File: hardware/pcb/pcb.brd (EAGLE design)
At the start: 100 x 80 mm, 18 parts, among them IC1 LM1117MPX-ADJ

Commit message: added support for new new display
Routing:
- net GND: track 0.00 -> 10.2 mm
- net N$11: track 0.00 -> 1.84 mm
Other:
- board size 100 x 80 mm -> 51.7 x 80 mm
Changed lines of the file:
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@@
 <board>
 <plain>
-<wire x1="0" y1="0" x2="100" y2="0" width="0" layer="20"/>
+<wire x1="48.26" y1="0" x2="100" y2="0" width="0" layer="20"/>
 <wire x1="100" y1="0" x2="100" y2="80" width="0" layer="20"/>
-<wire x1="100" y1="80" x2="0" y2="80" width="0" layer="20"/>
-<wire x1="0" y1="80" x2="0" y2="0" width="0" layer="20"/>
+<wire x1="100" y1="80" x2="48.26" y2="80" width="0" layer="20"/>
+<wire x1="48.26" y1="80" x2="48.26" y2="0" width="0" layer="20"/>
 </plain>
 <attributes>
@@
 <contactref element="JP3" pad="1"/>
 <contactref element="SV2" pad="4"/>
-<wire x1="94.535" y1="72.36" x2="97.36" y2="77.385" width="0" layer="19" extent="16-16"/>
-<wire x1="97.36" y1="69.935" x2="94.535" y2="72.36" width="0" layer="19" extent="16-16"/>
+<wire x1="94.535" y1="72.36" x2="96.55" y2="72.36" width="0.1524" layer="16"/>
+<wire x1="96.55" y1="72.36" x2="97.409" y2="71.501" width="0.1524" layer="16"/>
+<wire x1="97.409" y1="71.501" x2="97.409" y2="69.984" width="0.1524" layer="16"/>
+<wire x1="97.409" y1="69.984" x2="97.36" y2="69.935" width="0.1524" layer="16"/>
+<wire x1="97.36" y1="77.385" x2="97.36" y2="73.17" width="0.1524" layer="16"/>
+<wire x1="97.36" y1="73.17" x2="96.55" y2="72.36" width="0.1524" layer="16"/>
 <wire x1="95.25" y1="46.04" x2="97.36" y2="69.935" width="0" layer="19" extent="16-16"/>
 <wire x1="83.51" y1="42.45" x2="95.25" y2="46.04" width="0" layer="19" extent="16-16"/>
@@
 <wire x1="55.62" y1="17.53" x2="55.62" y2="45.47" width="0" layer="19" extent="1-1"/>
 <wire x1="55.62" y1="12.45" x2="55.62" y2="17.53" width="0" layer="19" extent="1-1"/>
+<wire x1="59.69" y1="11.43" x2="55.62" y2="12.45" width="0" layer="19" extent="1-1"/>
 <wire x1="55.62" y1="7.37" x2="55.62" y2="12.45" width="0" layer="19" extent="1-1"/>
-<wire x1="63.82" y1="5.08" x2="55.62" y2="7.37" width="0" layer="19" extent="16-16"/>
-<wire x1="65.72" y1="7.62" x2="63.82" y2="5.08" width="0" layer="19" extent="16-16"/>
-<wire x1="59.69" y1="11.43" x2="55.62" y2="7.37" width="0" layer="19" extent="1-1"/>
+<wire x1="65.72" y1="7.62" x2="59.69" y2="11.43" width="0" layer="19" extent="16-16"/>
+<wire x1="63.82" y1="5.08" x2="65.72" y2="7.62" width="0" layer="19" extent="16-16"/>
 </signal>
 <signal name="N$1">
@@
 <contactref element="IC1" pad="3"/>
 <contactref element="C1" pad="1"/>
-<wire x1="69.291" y1="72.161" x2="94.535" y2="74.96" width="0" layer="19" extent="16-16"/>
+<wire x1="94.535" y1="74.96" x2="94.505" y2="74.93" width="0.1524" layer="16"/>
+<wire x1="94.505" y1="74.93" x2="92.71" y2="74.93" width="0.1524" layer="16"/>
+<wire x1="69.291" y1="72.161" x2="92.71" y2="74.93" width="0" layer="19" extent="16-16"/>
 <wire x1="65.72" y1="5.08" x2="69.291" y2="72.161" width="0" layer="19" extent="16-16"/>
 </signal>

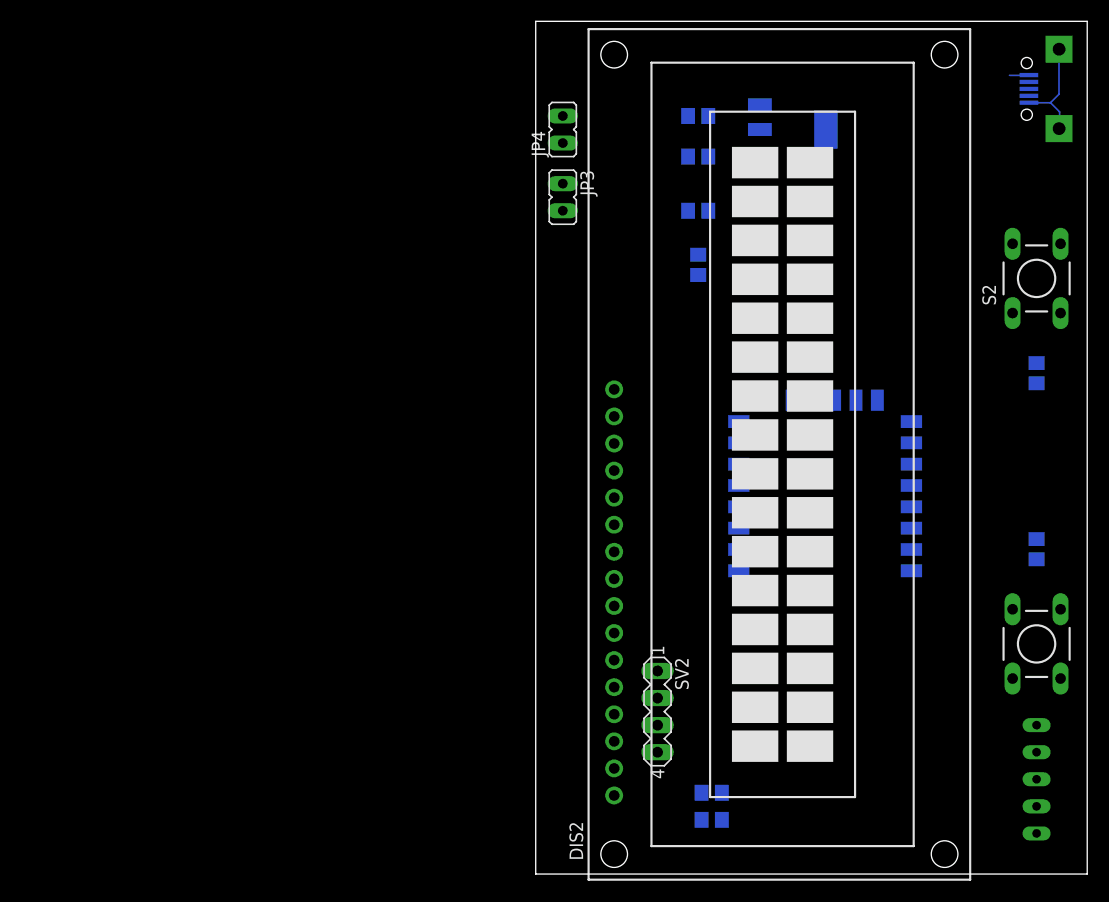
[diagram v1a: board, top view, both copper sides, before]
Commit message: debugged pcb, which is now working
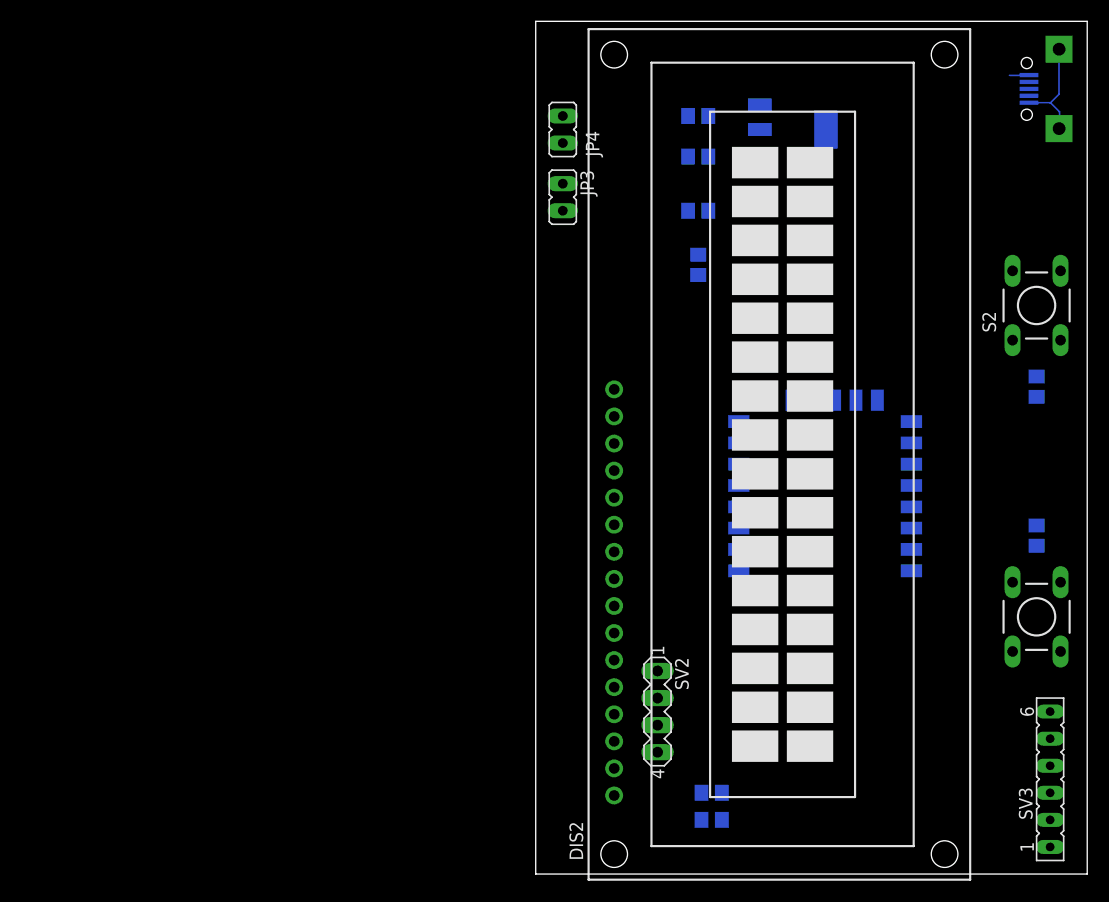
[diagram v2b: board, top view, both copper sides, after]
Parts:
- removed SV1: (no value), con-lsta:FE05-1
- added SV3: (no value), con-lsta:FE06
- moved S1 2.54 mm to (95.2, 24.1)
- moved S2 2.54 mm to (95.2, 53.3)
- moved R3 1.27 mm to (95.2, 45.7)
- moved R1 1.27 mm to (95.2, 31.8)
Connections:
- net GND: now also SV3.1; no longer SV1.2
- net N$1: now also SJR1.14, SV2.2; no longer SJR1.5
- net N$10: now also SV3.5; no longer SV1.3
- net N$5: no longer SV2.2
- net N$7: now also SJR1.5; no longer SJR1.14
- net N$9: now also SV3.4; no longer SV1.4
